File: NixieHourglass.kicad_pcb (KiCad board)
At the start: 2 copper layers, 26 parts, among them J1 Conn_02x05_Odd_Even, J3 VBAT_OUT, J4 HV_IN, Q1 Q_NPN_BEC, Q2 MMBTA42, Q3 MMBTA42, SW1 SKRPACE010, SW2 SKRPACE010, U1 ATmega328P-AU, U2 DS3231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

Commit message: routing
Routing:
- net /NIX_0: track 6.21 -> 47.6 mm
- net /NIX_2: track 0.00 -> 40.6 mm
- net /NIX_3: track 2.82 -> 12.5 mm, vias 0 -> 2
- net /NIX_1: track 24.8 -> 25.9 mm
- net /NIX_5: track 13.9 -> 14.9 mm
- net /NIX_4: track 11.0 -> 11.6 mm

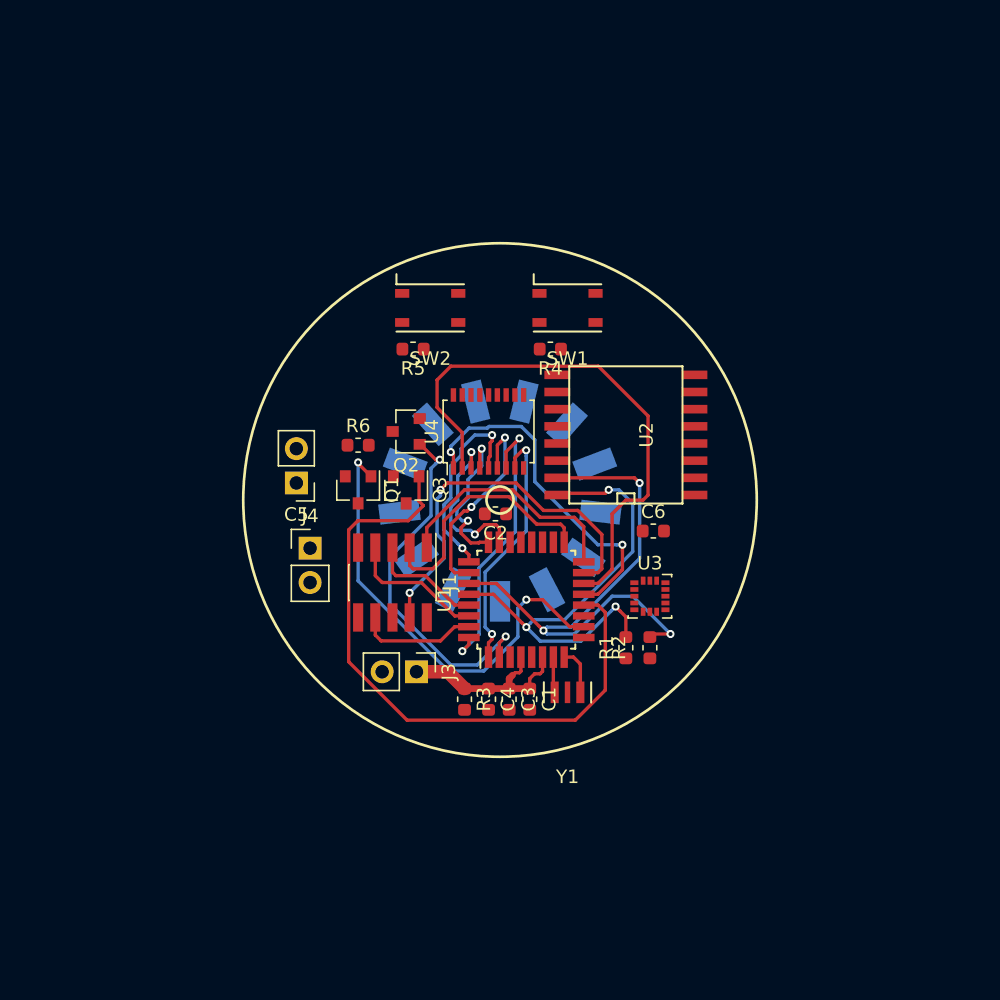
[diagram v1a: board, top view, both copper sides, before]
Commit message: add zener
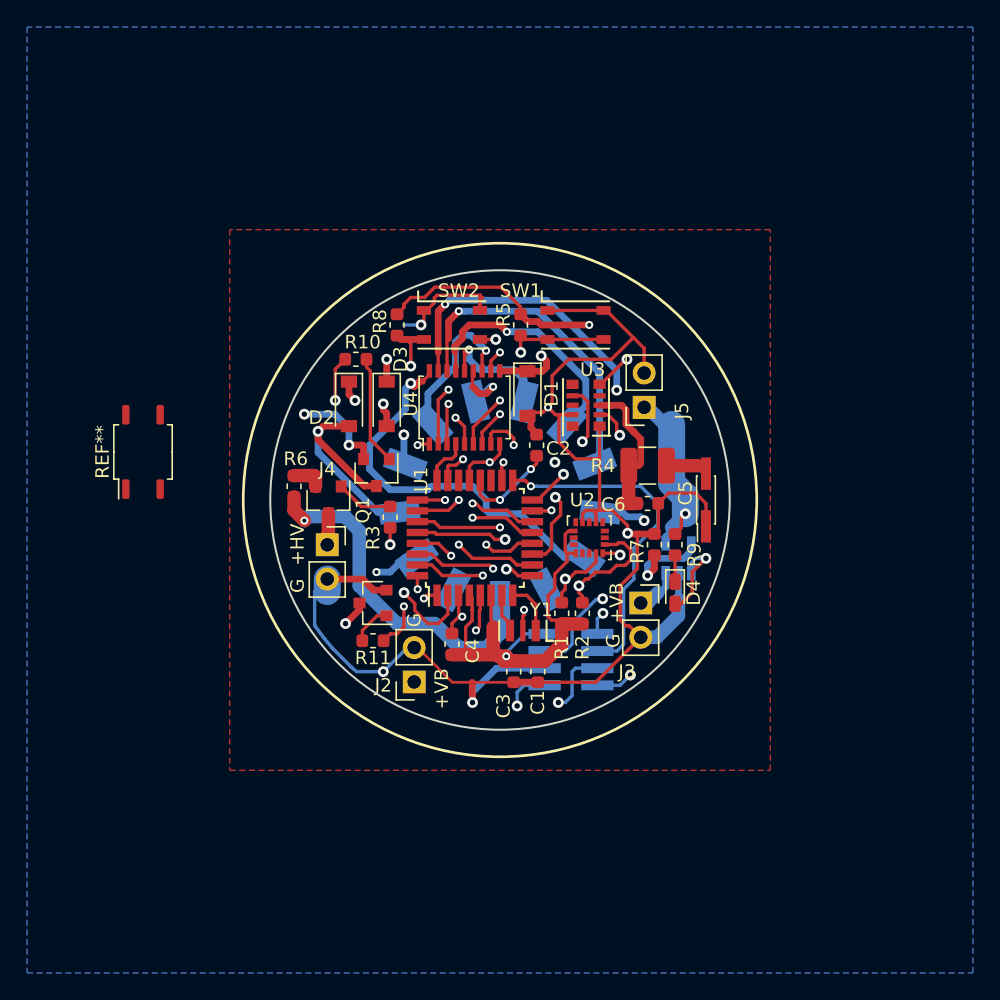
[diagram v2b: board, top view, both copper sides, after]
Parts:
- added D1: Zener_47V, Diode_SMD:D_SOD-123, F.Cu at (92.0, 72.1)
- added D2: GS1010FL, Diode_SMD:D_SOD-123, F.Cu at (78.8, 72.9)
- added D3: GS1010FL, Diode_SMD:D_SOD-123, F.Cu at (81.6, 72.9)
- added D4: LED, LED_SMD:LED_0603_1608Metric_Castellated, F.Cu at (103.0, 86.9)
- added J2: VBAT_OUT, Connector_PinSocket_2.54mm:PinSocket_1x02_P2.54mm_Vertical, F.Cu at (83.7, 93.5)
- added J5: CHG_IN, Connector_PinSocket_2.54mm:PinSocket_1x02_P2.54mm_Vertical, F.Cu at (100.7, 73.1)
- added R10: 10k, R_SMD:R_0603_1608Metric, F.Cu at (79.3, 69.6)
- added R11: 10k, R_SMD:R_0603_1608Metric, F.Cu at (80.6, 90.4)
- added R7: R, R_SMD:R_0603_1608Metric, F.Cu at (101.4, 83.3)
- added R8: 10k, R_SMD:R_0603_1608Metric, F.Cu at (82.4, 67.0)
- added R9: R, R_SMD:R_0603_1608Metric, F.Cu at (103.0, 83.3)
- added REF**: SOP-4_3.8x4.1mm_P2.54mm, Package_SO:SOP-4_3.8x4.1mm_P2.54mm, F.Cu at (63.6, 76.4)
- added U5: MCP73832T-2ACI_OT, TO_SOT_SMD:SOT-23-5, B.Cu at (103.2, 84.3)
- C5: footprint Connector_PinHeader_2.54mm:PinHeader_1x02_P2.54mm_Vertical -> Connector_PinHeader_1.27mm:PinHeader_2x01_P1.27mm_Vertical_SMD
- J1: value Conn_02x05_Odd_Even -> Conn_02x04_Odd_Even; footprint Pin_Headers:Pin_Header_Straight_2x05_Pitch1.27mm_SMD -> Connector_PinHeader_1.27mm:PinHeader_2x04_P1.27mm_Vertical_SMD; moved to B.Cu
- J3: value VBAT_OUT -> VBAT_IN; footprint Pin_Headers:Pin_Header_Straight_1x02_Pitch2.54mm -> Connector_PinSocket_2.54mm:PinSocket_1x02_P2.54mm_Vertical
- J4: footprint Pin_Headers:Pin_Header_Straight_1x02_Pitch2.54mm -> Connector_PinSocket_2.54mm:PinSocket_1x02_P2.54mm_Vertical
- R4: value 10k -> 1210_ROHM_MCR25JZHJ101; footprint Resistor_SMD:R_0603_1608Metric -> R_SMD:R_1210_3225Metric
- U2: value DS3231 -> LIS3DHTR; footprint SMD_Packages:SO-16-L -> Package_LGA:LGA-16_3x3mm_P0.5mm_LayoutBorder3x5y
- U3: value LIS3DHTR -> RX8900CE; footprint Package_LGA:LGA-16_3x3mm_P0.5mm_LayoutBorder3x5y -> NixieHourGlass:RX8900CE
- moved C5 30.3 mm to (105.2, 80.0), turned to 90 degrees
- moved J3 17.4 mm to (100.4, 87.6), turned to 0 degrees
- moved R3 14.6 mm to (81.9, 81.3)
- moved J1 14.4 mm to (95.3, 91.8), turned to 180 degrees
- moved U3 13.1 mm to (97.4, 74.5), turned to 180 degrees
- moved R4 11.2 mm to (100.9, 77.5)
- moved Q3 8.72 mm to (80.6, 87.6), turned to 180 degrees
- moved R5 8.16 mm to (91.5, 67.0), turned to 270 degrees
- moved U2 8.08 mm to (96.6, 82.8)
- moved U1 5.95 mm to (88.1, 82.8)
- moved C2 5.92 mm to (92.7, 75.9), turned to 90 degrees
- moved Y1 5.64 mm to (91.7, 89.7)
- moved R6 5.63 mm to (74.8, 79.0), turned to 270 degrees
- moved R2 5.61 mm to (96.1, 88.4)
- moved R1 5.38 mm to (94.6, 88.4)
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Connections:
- C5 pad 2: +BATT -> Net-(C5-Pad2)
- C6 pad 1: +BATT -> Net-(C6-Pad1)
- Q1 pad 1: /NIX_ANODE -> Net-(Q1-Pad1)
- Q2 pad 1: /NIX_9 -> Net-(Q2-Pad1)
- Q3 pad 1: /NIX_0 -> Net-(Q3-Pad1)
- R1 pad 2: /SCL -> SCL
- R2 pad 2: /SDA -> SDA
- R3 pad 1: +BATT -> Net-(Q1-Pad1)
- R3 pad 2: /RESET -> /NIX_ANODE
- R4 pad 1: +BATT -> Net-(C5-Pad2)
- R4 pad 2: Net-(R4-Pad2) -> Net-(C6-Pad1)
- R5 pad 2: Net-(R5-Pad2) -> SW_0
- SW1 pad 3: Net-(R4-Pad2) -> SW_0
- SW1 pad 4: Net-(R4-Pad2) -> SW_0
- SW2 pad 3: Net-(R5-Pad2) -> SW_1
- SW2 pad 4: Net-(R5-Pad2) -> SW_1
- U1 pad 11: (no net) -> SW_1
- U1 pad 27: /SDA -> SDA
- U1 pad 28: /SCL -> SCL
- U1 pad 9: (no net) -> SW_0
- U2 pad 1: (no net) -> +BATT
- U2 pad 10: (no net) -> GND
- U2 pad 12: (no net) -> GND
- U2 pad 13: GND -> (no net)
- U2 pad 15: /SDA -> (no net)
- U2 pad 16: /SCL -> (no net)
- U2 pad 2: +BATT -> (no net)
- U2 pad 4: +BATT -> SCL
- U2 pad 5: (no net) -> GND
- U2 pad 6: (no net) -> SDA
- U3 pad 1: +BATT -> GND
- U3 pad 10: GND -> (no net)
- U3 pad 2: (no net) -> +BATT
- U3 pad 3: (no net) -> Net-(C6-Pad1)
- U3 pad 4: /SCL -> (no net)
- U3 pad 5: GND -> SCL
- U3 pad 6: /SDA -> (no net)
- U3 pad 7: (no net) -> SDA
- U3 pad 9: (no net) -> GND
- U4 pad 10: (no net) -> Net-(D1-Pad1)
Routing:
- net GND: track 0.00 -> 177.9 mm, vias 0 -> 12
- net +BATT: track 15.0 -> 116.8 mm, vias 0 -> 4
- net SCL: track 0.00 -> 42.6 mm, vias 0 -> 3
- net /SDA: track 41.6 -> 0.00 mm, vias 3 -> 0
- net SDA: track 0.00 -> 38.6 mm, vias 0 -> 3
- net Net-(N1-Pad2): track 0.00 -> 37.0 mm, vias 0 -> 3
- net /SCL: track 35.8 -> 0.00 mm, vias 3 -> 0
- net SW_1: track 0.00 -> 33.7 mm, vias 0 -> 3
- net /NIX_0: track 47.6 -> 16.0 mm, vias 0 -> 2
- net Net-(N1-Pad1): track 0.00 -> 29.7 mm, vias 0 -> 1
- net SW_0: track 0.00 -> 28.5 mm, vias 0 -> 3
- net Net-(N1-PadA): track 0.00 -> 26.7 mm, vias 0 -> 1
- net Net-(D1-Pad1): track 0.00 -> 26.7 mm, vias 0 -> 3
- net Net-(D3-Pad2): track 0.00 -> 24.5 mm, vias 0 -> 3
- net Net-(N1-Pad3): track 0.00 -> 24.0 mm, vias 0 -> 1
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- added copper zone on In2.Cu, net +BATT
- added copper zone on B.Cu, net GND
- added copper zone on F.Cu, net GND
- added copper zone on In1.Cu, net GND
- added copper zone on In2.Cu, net GND
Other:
- board outline added: 34 x 34 mm
- copper layers 2 -> 4
- net class 0.5mm: clearance 0.2 -> 0.25
- net class 1.0mm: clearance 0.2 -> 0.25
- net class 2.0mm: clearance 0.2 -> 0.25
- net class 5.0mm added: clearance 0.25, trace_width 5, via_dia 0.8, via_drill 0.4
- net class Default: clearance 0.2 -> 0.25; via_dia 0.6 -> 0.8; via_drill 0.3 -> 0.4
- rule trace_clearance: 0.2 -> 0.25
- board text added: "+HV"
- board text added: "+VB"
- board text added: "G"
- board text added: "Hourglass"
- board text added: "v0.2"

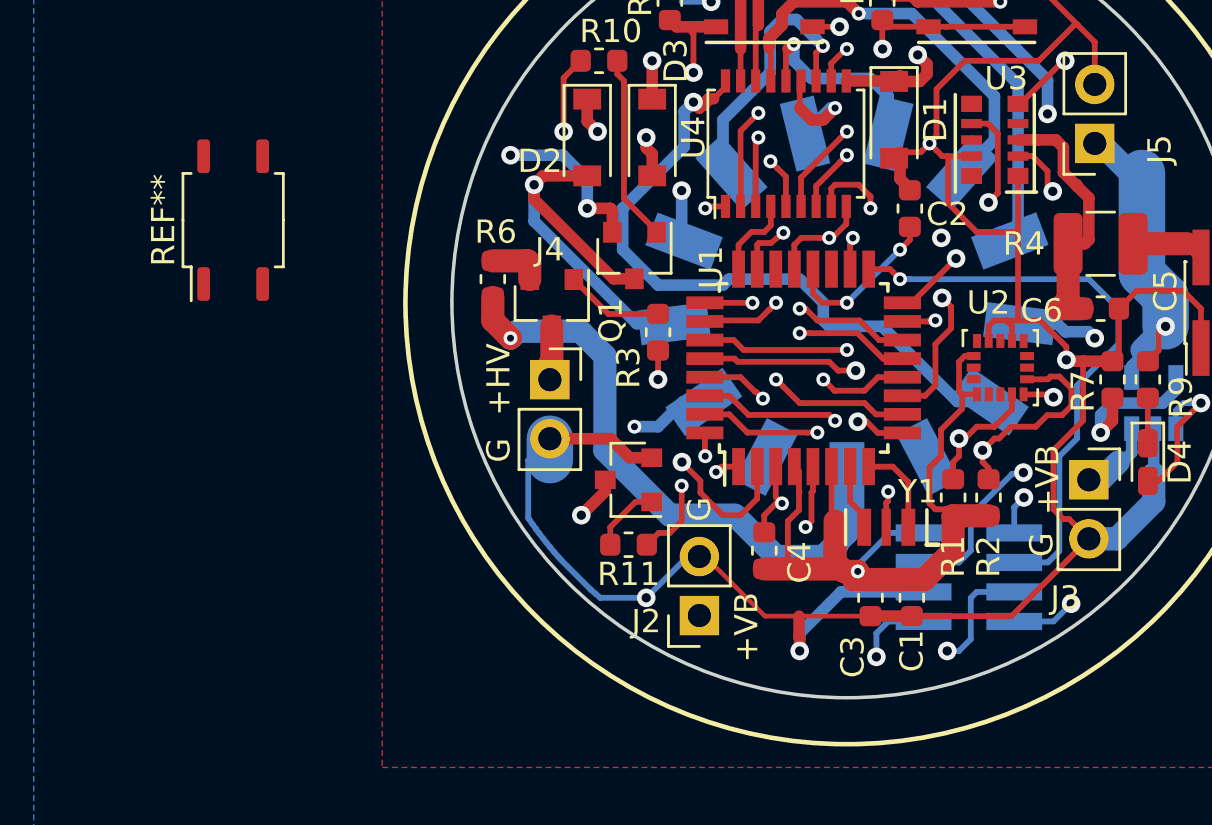
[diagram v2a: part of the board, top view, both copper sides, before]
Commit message: Add optocoupler
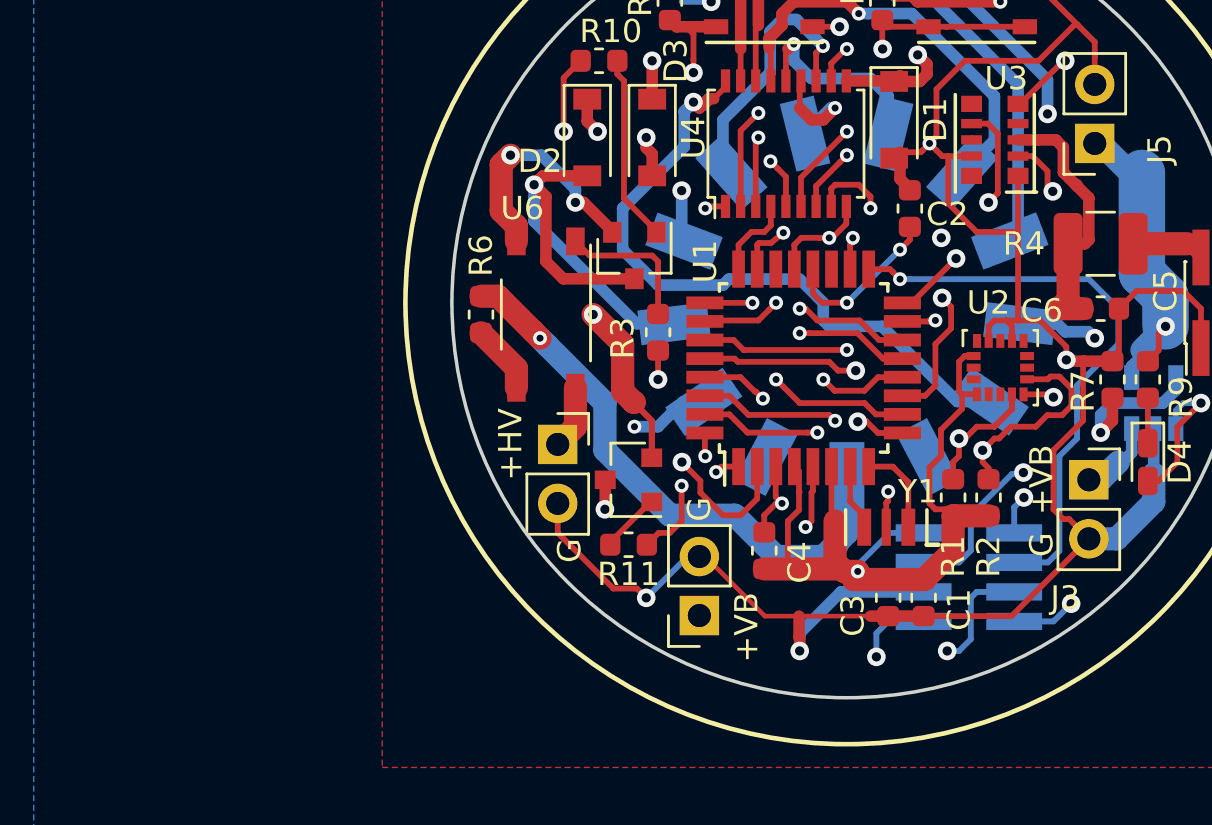
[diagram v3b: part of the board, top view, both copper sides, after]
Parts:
- removed Q1: Q_NPN_BEC, TO_SOT_SMD:SOT-23
- removed REF**: SOP-4_3.8x4.1mm_P2.54mm, Package_SO:SOP-4_3.8x4.1mm_P2.54mm
- added U6: TLP127, Package_SO:MFSOP6-4_4.4x3.6mm_P1.27mm, F.Cu at (77.0, 80.5)
- R3: value 10k -> 220
- moved J4 2.80 mm to (77.6, 86.1)
- moved R6 1.61 mm to (74.3, 80.5), turned to 90 degrees
- moved C3 0.76 mm to (91.8, 92.7)
- moved C1 0.51 mm to (93.3, 92.7)
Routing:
- net GND: track 177.9 -> 194.3 mm, vias 12 -> 13
- net Net-(R3-Pad1): track 4.24 -> 6.17 mm
- net Net-(N1-PadA): track 26.7 -> 25.2 mm
- net Net-(D3-Pad2): track 24.5 -> 23.2 mm
- net Net-(D2-Pad2): track 18.2 -> 19.5 mm
- net Net-(R6-Pad1): track 2.34 -> 2.99 mm
